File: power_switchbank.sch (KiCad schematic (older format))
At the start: 0 parts

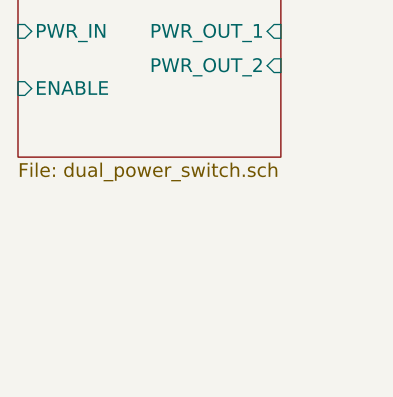
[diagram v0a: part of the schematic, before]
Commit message: add 5v power switch
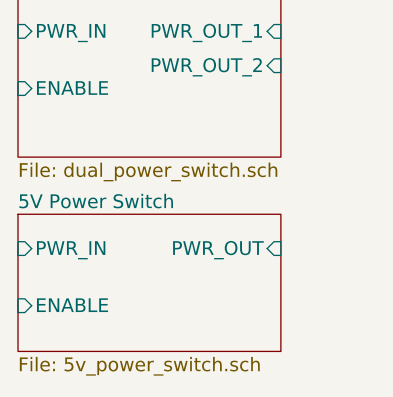
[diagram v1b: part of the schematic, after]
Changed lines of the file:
@@
 $Descr A4 11693 8268
 encoding utf-8
-Sheet 4 6
+Sheet 4 7
 Title "Power Switch Bank"
 Date "2017-07-02"
@@
 F5 "PWR_OUT_2" I R 4250 1900 60
 $EndSheet
+$Sheet
+S 3100 2550 1150 600
+U 59616167
+F0 "5V Power Switch" 60
+F1 "5v_power_switch.sch" 60
+F2 "PWR_IN" I L 3100 2700 60
+F3 "ENABLE" I L 3100 2950 60
+F4 "PWR_OUT" I R 4250 2700 60
+$EndSheet
 $EndSCHEMATC

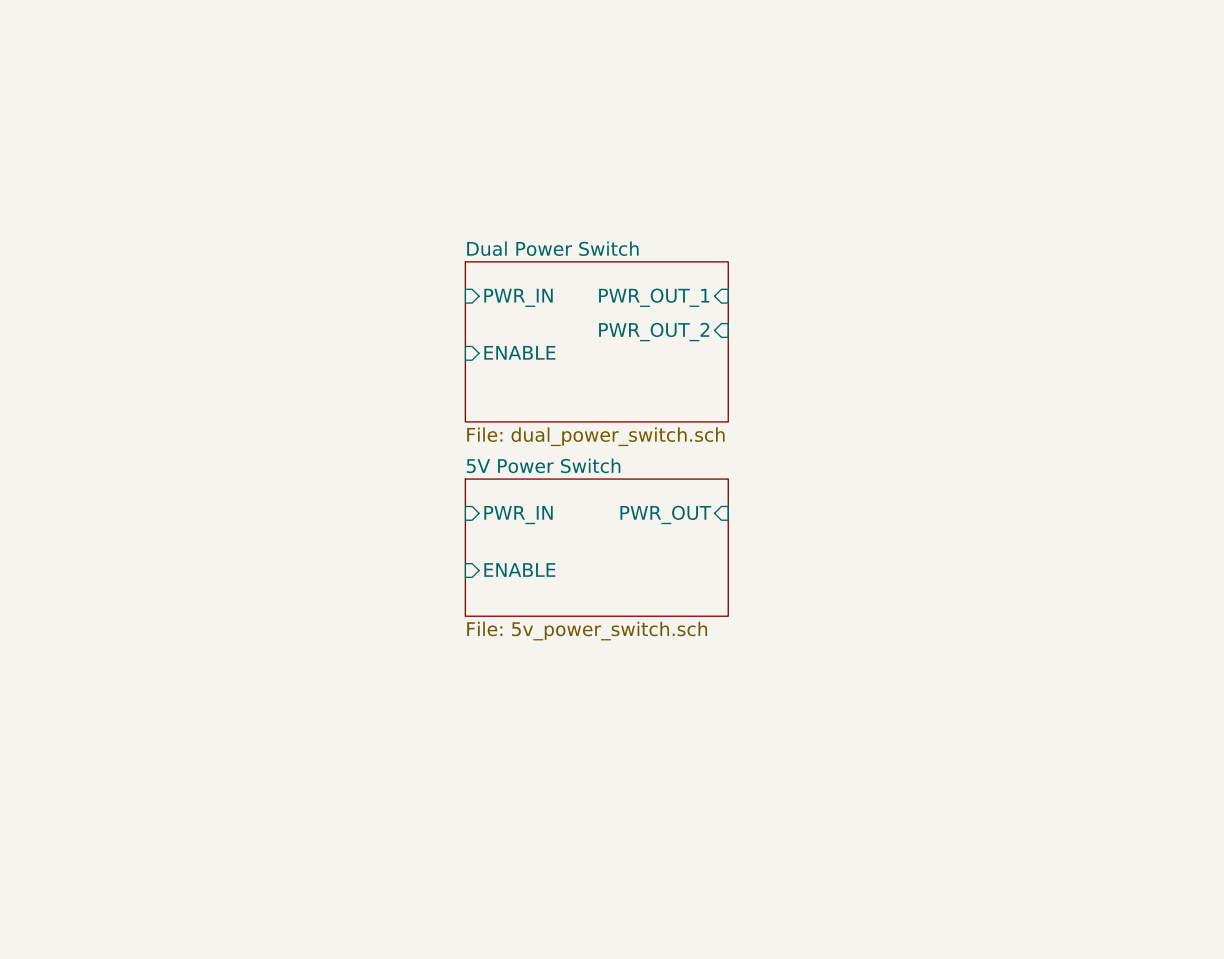
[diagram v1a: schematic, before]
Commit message: add high power switch
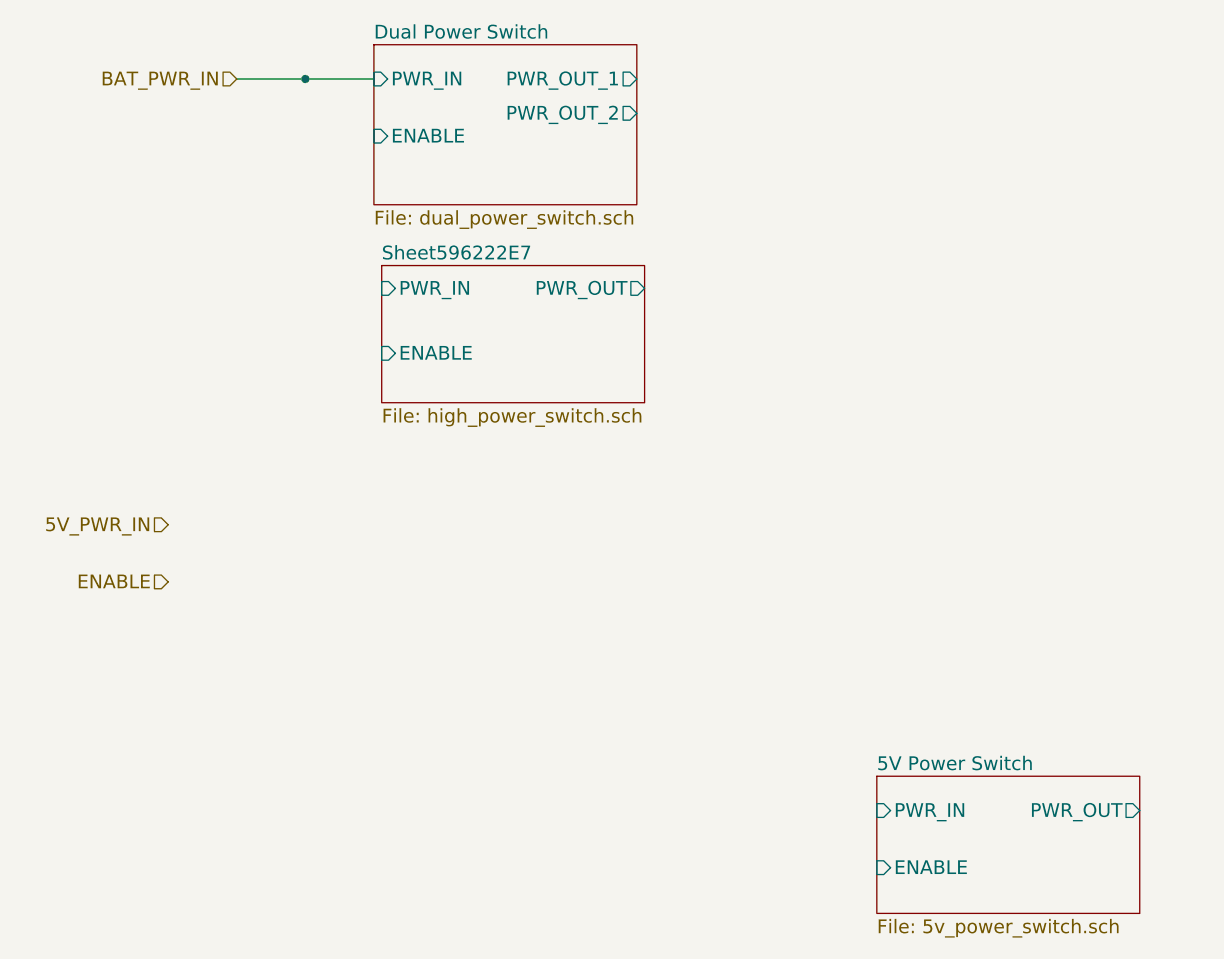
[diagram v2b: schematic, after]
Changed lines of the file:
@@
 LIBS:valves
 LIBS:ltc1473
-LIBS:agg-kicad
 LIBS:nmos_sssgd
 LIBS:ehhd015a0a
@@
 LIBS:tps2024d
 LIBS:its5215l
+LIBS:agg-kicad
 LIBS:pdb-cache
 EELAYER 25 0
@@
 $Descr A4 11693 8268
 encoding utf-8
-Sheet 4 7
+Sheet 4 8
 Title "Power Switch Bank"
 Date "2017-07-02"
@@
 $EndDescr
 $Sheet
-S 3100 1600 1150 700
+S 2700 650  1150 700
 U 59613F99
 F0 "Dual Power Switch" 60
 F1 "dual_power_switch.sch" 60
-F2 "PWR_IN" I L 3100 1750 60
-F3 "ENABLE" I L 3100 2000 60
-F4 "PWR_OUT_1" I R 4250 1750 60
-F5 "PWR_OUT_2" I R 4250 1900 60
+F2 "PWR_IN" I L 2700 800 60
+F3 "ENABLE" I L 2700 1050 60
+F4 "PWR_OUT_1" O R 3850 800 60
+F5 "PWR_OUT_2" O R 3850 950 60
 $EndSheet
 $Sheet
-S 3100 2550 1150 600
+S 4900 3850 1150 600
 U 59616167
 F0 "5V Power Switch" 60
 F1 "5v_power_switch.sch" 60
-F2 "PWR_IN" I L 3100 2700 60
-F3 "ENABLE" I L 3100 2950 60
-F4 "PWR_OUT" I R 4250 2700 60
+F2 "PWR_IN" I L 4900 4000 60
+F3 "ENABLE" I L 4900 4250 60
+F4 "PWR_OUT" O R 6050 4000 60
+$EndSheet
+Text HLabel 2100 800  0    60   Input ~ 0
+BAT_PWR_IN
+Text HLabel 1800 2750 0    60   Input ~ 0
+5V_PWR_IN
+Text HLabel 1800 3000 0    60   Input ~ 0
+ENABLE
+Connection ~ 2400 800
+Wire Wire Line
+	2100 800  2700 800
+$Sheet
+S 2734 1616 1150 600
+U 596222E8
+F0 "Sheet596222E7" 60
+F1 "high_power_switch.sch" 60
+F2 "PWR_IN" I L 2734 1716 60
+F3 "PWR_OUT" O R 3884 1716 60
+F4 "ENABLE" I L 2734 2000 60
 $EndSheet
 $EndSCHEMATC

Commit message: clean up
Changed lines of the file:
@@
 $EndSheet
 $Sheet
-S 4900 3850 1150 600
+S 2750 2750 1150 600
 U 59616167
 F0 "5V Power Switch" 60
 F1 "5v_power_switch.sch" 60
-F2 "PWR_IN" I L 4900 4000 60
-F3 "ENABLE" I L 4900 4250 60
-F4 "PWR_OUT" O R 6050 4000 60
+F2 "PWR_IN" I L 2750 2900 60
+F3 "ENABLE" I L 2750 3150 60
+F4 "PWR_OUT" O R 3900 2900 60
 $EndSheet
 Text HLabel 2100 800  0    60   Input ~ 0
@@
 Text HLabel 1800 3000 0    60   Input ~ 0
 ENABLE
-Connection ~ 2400 800
-Wire Wire Line
-	2100 800  2700 800
 $Sheet
 S 2734 1616 1150 600
 U 596222E8
-F0 "Sheet596222E7" 60
+F0 "High Power Switch" 60
 F1 "high_power_switch.sch" 60
 F2 "PWR_IN" I L 2734 1716 60

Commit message: more cleaning
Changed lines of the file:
@@
 $Descr A4 11693 8268
 encoding utf-8
-Sheet 4 8
+Sheet 4 9
 Title "Power Switch Bank"
 Date "2017-07-02"
@@
 $EndDescr
 $Sheet
-S 2700 650  1150 700
+S 3000 3750 1150 700
 U 59613F99
 F0 "Dual Power Switch" 60
 F1 "dual_power_switch.sch" 60
-F2 "PWR_IN" I L 2700 800 60
-F3 "ENABLE" I L 2700 1050 60
-F4 "PWR_OUT_1" O R 3850 800 60
-F5 "PWR_OUT_2" O R 3850 950 60
+F2 "PWR_IN" I L 3000 3900 60
+F3 "ENABLE" I L 3000 4150 60
+F4 "PWR_OUT_1" O R 4150 3900 60
+F5 "PWR_OUT_2" O R 4150 4050 60
 $EndSheet
 $Sheet
-S 2750 2750 1150 600
+S 3050 5300 1150 600
 U 59616167
 F0 "5V Power Switch" 60
 F1 "5v_power_switch.sch" 60
-F2 "PWR_IN" I L 2750 2900 60
-F3 "ENABLE" I L 2750 3150 60
-F4 "PWR_OUT" O R 3900 2900 60
+F2 "PWR_IN" I L 3050 5450 60
+F3 "ENABLE" I L 3050 5700 60
+F4 "PWR_OUT" O R 4200 5450 60
 $EndSheet
-Text HLabel 2100 800  0    60   Input ~ 0
+Text HLabel 1600 4750 0    60   Input ~ 0
 BAT_PWR_IN
-Text HLabel 1800 2750 0    60   Input ~ 0
+Text HLabel 1800 5550 0    60   Input ~ 0
 5V_PWR_IN
-Text HLabel 1800 3000 0    60   Input ~ 0
+Text HLabel 1800 5800 0    60   Input ~ 0
 ENABLE
 $Sheet
-S 2734 1616 1150 600
-U 596222E8
+S 2600 1900 1150 550
+U 596398D9
 F0 "High Power Switch" 60
 F1 "high_power_switch.sch" 60
-F2 "PWR_IN" I L 2734 1716 60
-F3 "PWR_OUT" O R 3884 1716 60
-F4 "ENABLE" I L 2734 2000 60
+F2 "PWR_OUT" O R 3750 2000 60
+F3 "PWR_IN" I L 2600 2000 60
+F4 "ENABLE" I L 2600 2250 60
 $EndSheet
 $EndSCHEMATC

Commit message: update title box
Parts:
- added J? (x12): CONN_02X01, symbol CONN_02X01
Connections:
- net 5V Power Switch/PWR_OUT: now also J?.1 (P1), J?.1 (P1)
- net Dual Power Switch/PWR_OUT_1: now also J?.1 (P1)
- net Dual Power Switch/PWR_OUT_2: now also J?.1 (P1)
- net High Power Switch/PWR_OUT: now also J?.1 (P1), J?.1 (P1), J?.1 (P1), J?.1 (P1), J?.1 (P1), J?.1 (P1)
- new net 5V Power Switch 2/PWR_OUT: J?.1 (P1), J?.1 (P1)
- new net PGND: J?.2 (P2), J?.2 (P2), J?.2 (P2), J?.2 (P2), J?.2 (P2), J?.2 (P2), J?.2 (P2), J?.2 (P2), J?.2 (P2), J?.2 (P2), J?.2 (P2), J?.2 (P2)
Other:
- note added: "IMU"
- note added: "Motor Controllers"
- note added: "Sonar"

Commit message: clean up after annotate
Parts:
- gave numbers to parts that had none: 12
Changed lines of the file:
@@
 Motor Controllers
 $Comp
-L CONN_02X01 J?
+L CONN_02X01 J7
 U 1 1 596418C8
 P 4250 3950
-F 0 "J?" H 4250 4050 50  0000 C CNN
+F 0 "J7" H 4250 4050 50  0000 C CNN
 F 1 "CONN_02X01" H 4250 3850 50  0000 C CNN
 F 2 "" H 4250 2750 50  0001 C CNN
@@
 Sonar
 $Comp
-L CONN_02X01 J?
+L CONN_02X01 J8
 U 1 1 5964217E
 P 4250 4300
-F 0 "J?" H 4250 4400 50  0000 C CNN
+F 0 "J8" H 4250 4400 50  0000 C CNN
 F 1 "CONN_02X01" H 4250 4200 50  0000 C CNN
 F 2 "" H 4250 3100 50  0001 C CNN
@@
 	7250 3000 7550 3000
 $Comp
-L CONN_02X01 J?
+L CONN_02X01 J1
 U 1 1 5964ACFE
 P 4250 3000
-F 0 "J?" H 4250 3000 50  0000 C CNN
+F 0 "J1" H 4250 3000 50  0000 C CNN
 F 1 "CONN_02X01" H 4250 2900 50  0001 C CNN
 F 2 "" H 4250 1800 50  0001 C CNN
@@
 $EndComp
 $Comp
-L CONN_02X01 J?
+L CONN_02X01 J2
 U 1 1 5964AE5F
 P 4250 3100
-F 0 "J?" H 4250 3100 50  0000 C CNN
+F 0 "J2" H 4250 3100 50  0000 C CNN
 F 1 "CONN_02X01" H 4250 3000 50  0001 C CNN
 F 2 "" H 4250 1900 50  0001 C CNN
@@
 $EndComp
 $Comp
-L CONN_02X01 J?
+L CONN_02X01 J3
 U 1 1 5964AEC7
 P 4250 3200
-F 0 "J?" H 4250 3200 50  0000 C CNN
+F 0 "J3" H 4250 3200 50  0000 C CNN
 F 1 "CONN_02X01" H 4250 3100 50  0001 C CNN
 F 2 "" H 4250 2000 50  0001 C CNN
@@
 $EndComp
 $Comp
-L CONN_02X01 J?
+L CONN_02X01 J4
 U 1 1 5964AF26
 P 4250 3300
-F 0 "J?" H 4250 3300 50  0000 C CNN
+F 0 "J4" H 4250 3300 50  0000 C CNN
 F 1 "CONN_02X01" H 4250 3200 50  0001 C CNN
 F 2 "" H 4250 2100 50  0001 C CNN
@@
 $EndComp
 $Comp
-L CONN_02X01 J?
+L CONN_02X01 J5
 U 1 1 5964AF84
 P 4250 3400
-F 0 "J?" H 4250 3400 50  0000 C CNN
+F 0 "J5" H 4250 3400 50  0000 C CNN
 F 1 "CONN_02X01" H 4250 3300 50  0001 C CNN
 F 2 "" H 4250 2200 50  0001 C CNN
@@
 $EndComp
 $Comp
-L CONN_02X01 J?
+L CONN_02X01 J6
 U 1 1 5964AFE5
 P 4250 3500
-F 0 "J?" H 4250 3500 50  0000 C CNN
+F 0 "J6" H 4250 3500 50  0000 C CNN
 F 1 "CONN_02X01" H 4250 3400 50  0001 C CNN
 F 2 "" H 4250 2300 50  0001 C CNN
@@
 $EndComp
 $Comp
-L CONN_02X01 J?
+L CONN_02X01 J9
 U 1 1 5964D475
 P 9300 3000
-F 0 "J?" H 9300 3000 50  0000 C CNN
+F 0 "J9" H 9300 3000 50  0000 C CNN
 F 1 "CONN_02X01" H 9300 2900 50  0001 C CNN
 F 2 "" H 9300 1800 50  0001 C CNN
@@
 $EndComp
 $Comp
-L CONN_02X01 J?
+L CONN_02X01 J10
 U 1 1 5964D5CC
 P 9300 3200
-F 0 "J?" H 9300 3200 50  0000 C CNN
+F 0 "J10" H 9300 3200 50  0000 C CNN
 F 1 "CONN_02X01" H 9300 3100 50  0001 C CNN
 F 2 "" H 9300 2000 50  0001 C CNN
@@
 $EndSheet
 $Comp
-L CONN_02X01 J?
+L CONN_02X01 J11
 U 1 1 59655A0B
 P 9300 3850
-F 0 "J?" H 9300 3850 50  0000 C CNN
+F 0 "J11" H 9300 3850 50  0000 C CNN
 F 1 "CONN_02X01" H 9300 3750 50  0001 C CNN
 F 2 "" H 9300 2650 50  0001 C CNN
@@
 $EndComp
 $Comp
-L CONN_02X01 J?
+L CONN_02X01 J12
 U 1 1 59655B0A
 P 9300 4050
-F 0 "J?" H 9300 4050 50  0000 C CNN
+F 0 "J12" H 9300 4050 50  0000 C CNN
 F 1 "CONN_02X01" H 9300 3950 50  0001 C CNN
 F 2 "" H 9300 2850 50  0001 C CNN
@@
 	5550 5100 10150 5100
 $Comp
-L PGND #PWR?
+L PGND #PWR12
 U 1 1 596573C9
 P 10150 5400
-F 0 "#PWR?" H 10020 5440 50  0001 L CNN
+F 0 "#PWR12" H 10020 5440 50  0001 L CNN
 F 1 "PGND" H 10150 5300 50  0000 C CNN
 F 2 "" H 10150 5400 60  0001 C CNN

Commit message: fix issue with incorrect symbol
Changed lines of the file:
@@
 $EndSheet
 Wire Wire Line
-	3600 3000 3900 3000
-Wire Wire Line
-	3900 3000 4000 3000
-Wire Wire Line
-	3900 3000 3900 3100
-Wire Wire Line
-	3900 3100 3900 3200
-Wire Wire Line
-	3900 3200 3900 3300
-Wire Wire Line
-	3900 3300 3900 3400
-Wire Wire Line
-	3900 3400 3900 3500
+	3600 3000 4000 3000
+Wire Wire Line
+	3900 3000 3900 3500
 Wire Wire Line
 	3900 3500 4000 3500
@@
 	4500 3000 5550 3000
 Wire Wire Line
-	5550 3000 5550 3100
-Wire Wire Line
-	5550 3100 5550 3200
-Wire Wire Line
-	5550 3200 5550 3300
-Wire Wire Line
-	5550 3300 5550 3400
-Wire Wire Line
-	5550 3400 5550 3500
-Wire Wire Line
-	5550 3500 5550 3950
-Wire Wire Line
-	5550 3950 5550 4300
-Wire Wire Line
-	5550 4300 5550 5100
+	5550 3000 5550 5100
 Wire Wire Line
 	4500 3100 5550 3100
@@
 	3600 4300 4000 4300
 Wire Wire Line
-	6850 3000 7250 3000
-Wire Wire Line
-	7250 3000 7550 3000
+	6850 3000 7550 3000
 $Comp
 L CONN_02X01 J1
@@
 $EndComp
 Wire Wire Line
-	8700 3000 8950 3000
-Wire Wire Line
-	8950 3000 9050 3000
+	8700 3000 9050 3000
 Wire Wire Line
 	8950 3000 8950 3200
@@
 	9550 3000 10150 3000
 Wire Wire Line
-	10150 3000 10150 3200
-Wire Wire Line
-	10150 3200 10150 3850
-Wire Wire Line
-	10150 3850 10150 4050
-Wire Wire Line
-	10150 4050 10150 5100
-Wire Wire Line
-	10150 5100 10150 5400
+	10150 3000 10150 5400
 Wire Wire Line
 	9550 3200 10150 3200
@@
 $EndComp
 Wire Wire Line
-	8700 3850 8950 3850
-Wire Wire Line
-	8950 3850 9050 3850
+	8700 3850 9050 3850
 Wire Wire Line
 	8950 3850 8950 4050
@@
 	5550 5100 10150 5100
 $Comp
-L PGND #PWR12
+L PGND #PWR012
 U 1 1 596573C9
 P 10150 5400
-F 0 "#PWR12" H 10020 5440 50  0001 L CNN
+F 0 "#PWR012" H 10020 5440 50  0001 L CNN
 F 1 "PGND" H 10150 5300 50  0000 C CNN
 F 2 "" H 10150 5400 60  0001 C CNN
@@
 Connection ~ 10150 5100
 Wire Wire Line
-	1850 4600 2050 4600
-Wire Wire Line
-	2050 4600 2050 4150
-Wire Wire Line
-	2050 4150 2050 3250
+	2050 4600 1850 4600
+Wire Wire Line
+	2050 3250 2050 4600
 Wire Wire Line
 	2050 3250 2450 3250
@@
 	7050 4600 6850 4600
 Wire Wire Line
-	7050 3250 7050 4100
-Wire Wire Line
-	7050 4100 7050 4600
+	7050 3250 7050 4600
 Wire Wire Line
 	7050 4100 7550 4100
